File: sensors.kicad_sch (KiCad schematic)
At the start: 98 parts, among them M1 CD74HC4067SM, M2 CD74HC4067SM, M3 CD74HC4067SM, M4 CD74HC4067SM, M5 CD74HC4067SM, M6 CD74HC4067SM

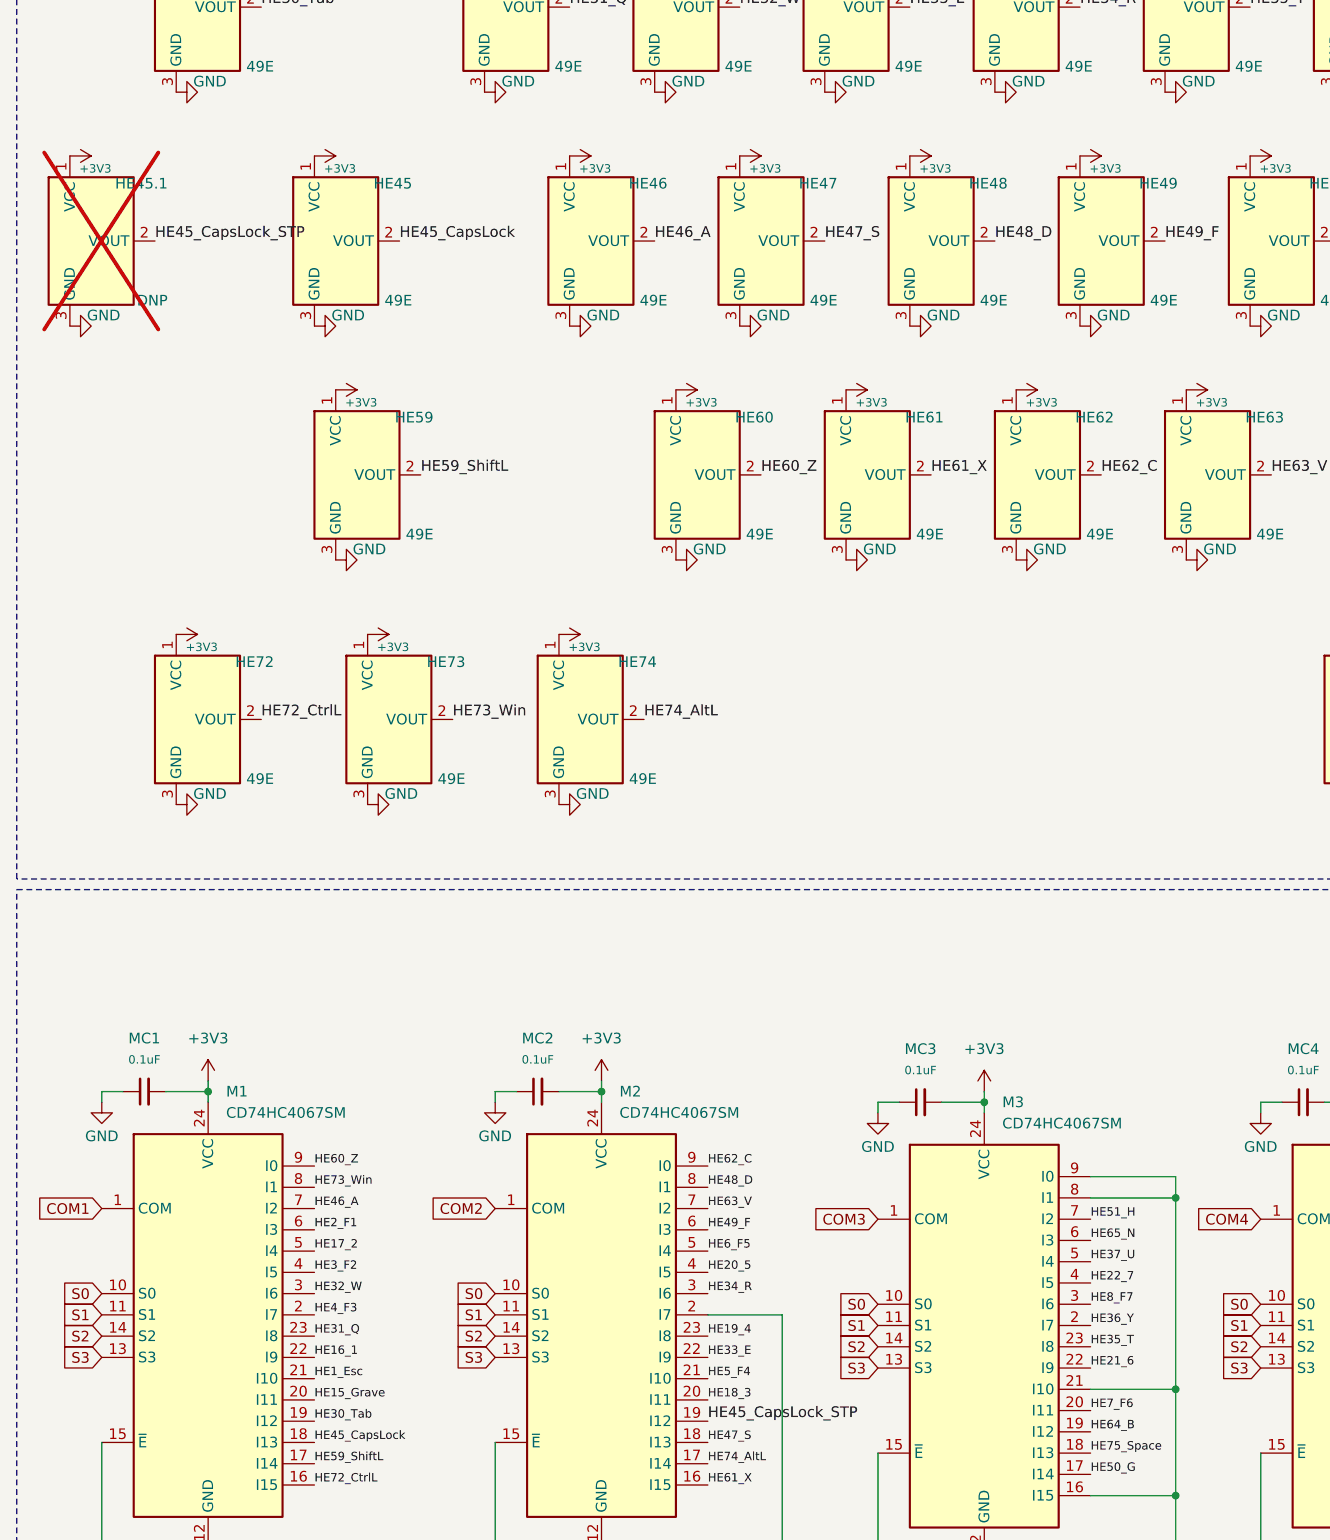
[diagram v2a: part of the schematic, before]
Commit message: VLT PCB rev: dual TFT connector, RKJXT1F42001 footprint, LED expansion header
- Add 12-pin TFT connector alongside existing 8-pin for CTP-integrated display option
- Superimpose RKJXT1F42001 5-way joystick footprint on EC11 encoder for testing
- Add LED expansion header for additional RGB zones
- Update production files
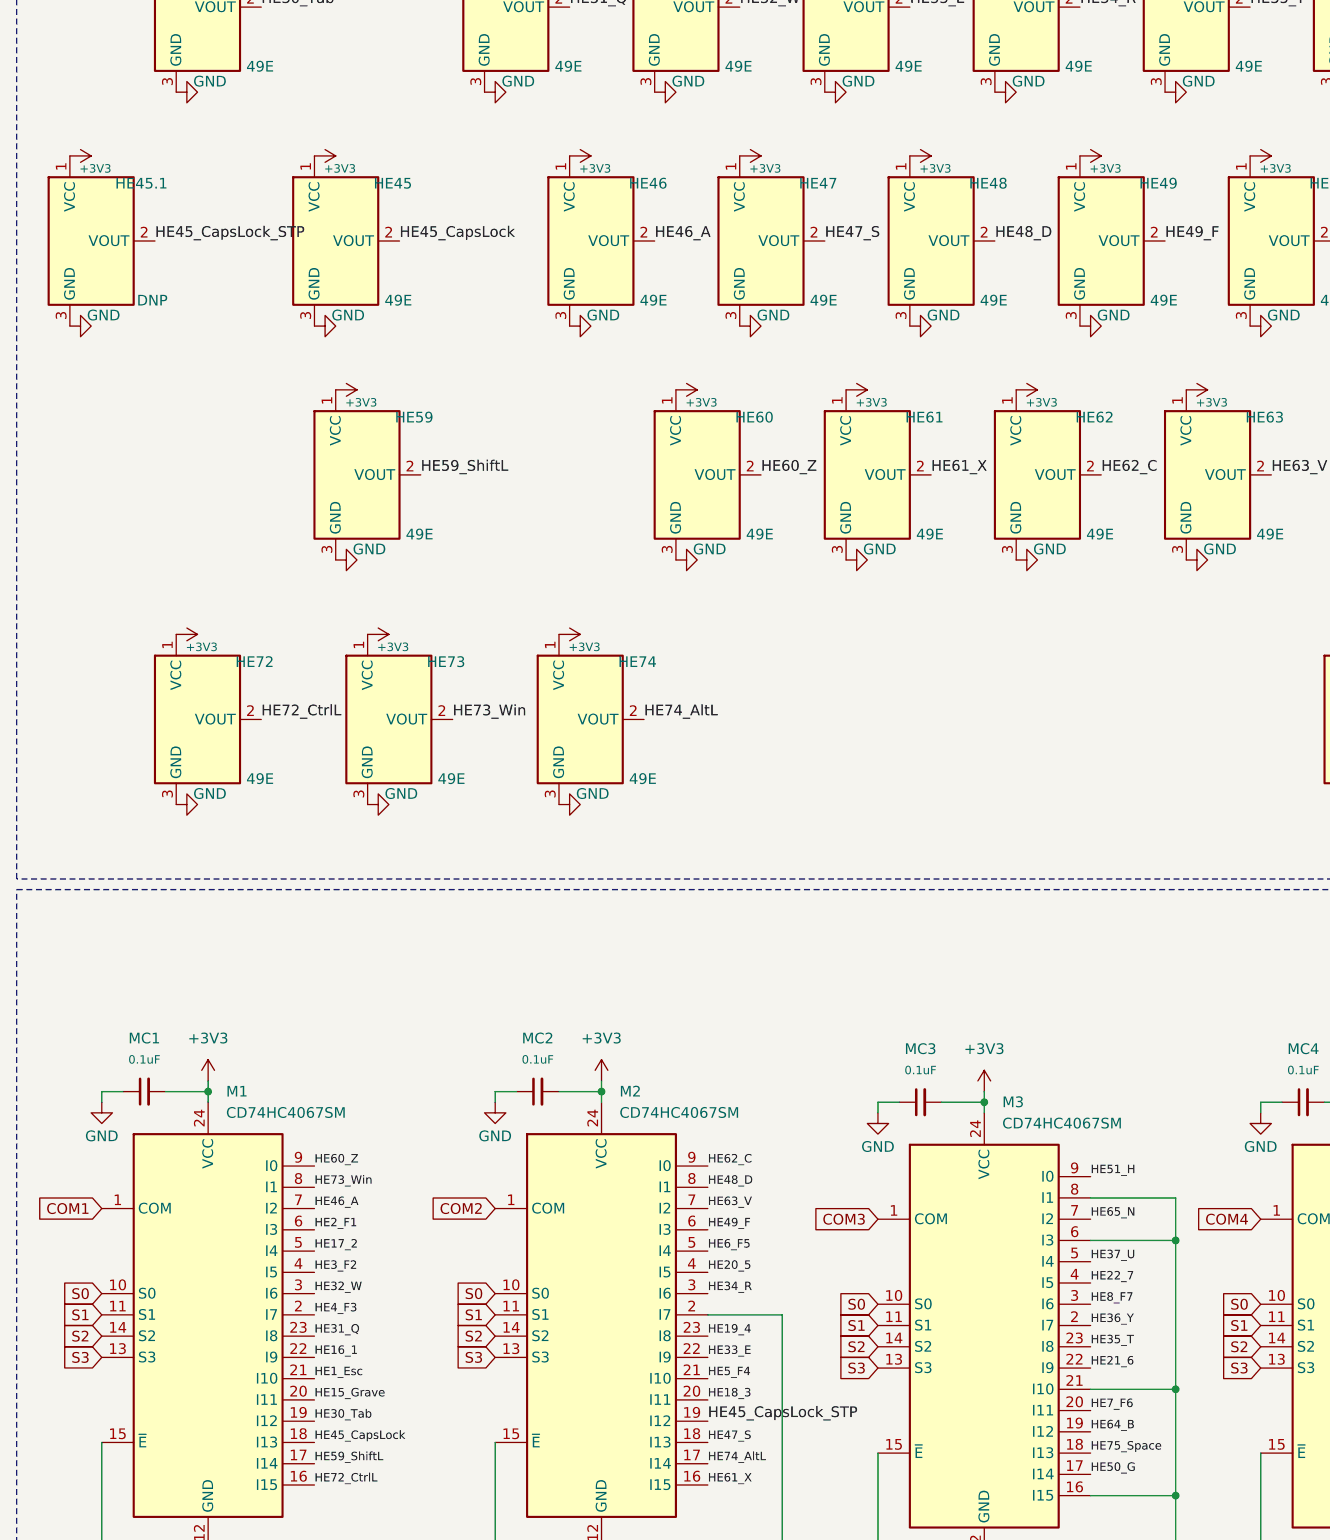
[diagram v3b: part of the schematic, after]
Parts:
- HE45.1: now fitted
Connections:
- net GND: now also M3.6 (I3); no longer M3.9 (I0)
- net HE51_H: now also M3.9 (I0); no longer M3.7 (I2)
- net HE65_N: now also M3.7 (I2); no longer M3.6 (I3)
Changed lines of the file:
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@@
 	)
 	(junction
-		(at 152.4 224.79)
-		(diameter 0)
-		(color 0 0 0 0)
-	)
-	(junction
 		(at 129.54 267.97)
 		(diameter 0)
@@
 	)
 	(junction
+		(at 152.4 229.87)
+		(diameter 0)
+		(color 0 0 0 0)
+	)
+	(junction
 		(at 196.85 227.33)
 		(diameter 0)
@@
 	(wire
 		(pts
-			(xy 152.4 222.25) (xy 152.4 224.79)
-		)
-		(stroke
-			(width 0)
-			(type default)
-		)
-	)
-	(wire
-		(pts
 			(xy 196.85 276.86) (xy 196.85 257.81)
 		)
@@
 	(wire
 		(pts
-			(xy 142.24 222.25) (xy 152.4 222.25)
-		)
-		(stroke
-			(width 0)
-			(type default)
-		)
-	)
-	(wire
-		(pts
 			(xy 96.52 238.76) (xy 105.41 238.76)
 		)
@@
 	(wire
 		(pts
+			(xy 142.24 229.87) (xy 152.4 229.87)
+		)
+		(stroke
+			(width 0)
+			(type default)
+		)
+	)
+	(wire
+		(pts
+			(xy 152.4 229.87) (xy 152.4 247.65)
+		)
+		(stroke
+			(width 0)
+			(type default)
+		)
+	)
+	(wire
+		(pts
 			(xy 162.56 267.97) (xy 175.26 267.97)
 		)
@@
 	(wire
 		(pts
-			(xy 152.4 224.79) (xy 152.4 247.65)
+			(xy 152.4 224.79) (xy 152.4 229.87)
 		)
 		(stroke
@@
 		)
 	)
+	(label "HE65_N"
+		(at 142.24 227.33 0)
+		(effects
+			(font
+				(size 1 1)
+			)
+			(justify left bottom)
+		)
+	)
 	(label "HE36_Y"
 		(at 181.61 82.55 0)
@@
 		)
 	)
-	(label "HE51_H"
-		(at 142.24 227.33 0)
-		(effects
-			(font
-				(size 1 1)
-			)
-			(justify left bottom)
-		)
-	)
 	(label "HE24_9"
 		(at 314.96 214.63 0)
@@
 		)
 	)
+	(label "HE51_H"
+		(at 142.24 222.25 0)
+		(effects
+			(font
+				(size 1 1)
+			)
+			(justify left bottom)
+		)
+	)
 	(label "HE32_W"
 		(at 49.53 236.22 0)
@@
 		)
 	)
-	(label "HE65_N"
-		(at 142.24 229.87 0)
-		(effects
-			(font
-				(size 1 1)
-			)
-			(justify left bottom)
-		)
-	)
 	(label "HE30_Tab"
 		(at 43.18 82.55 0)
@@
 		(in_bom yes)
 		(on_board yes)
-		(dnp yes)
+		(dnp no)
 		(property "Reference" "HE45.1"
 			(at 32.004 103.632 0)

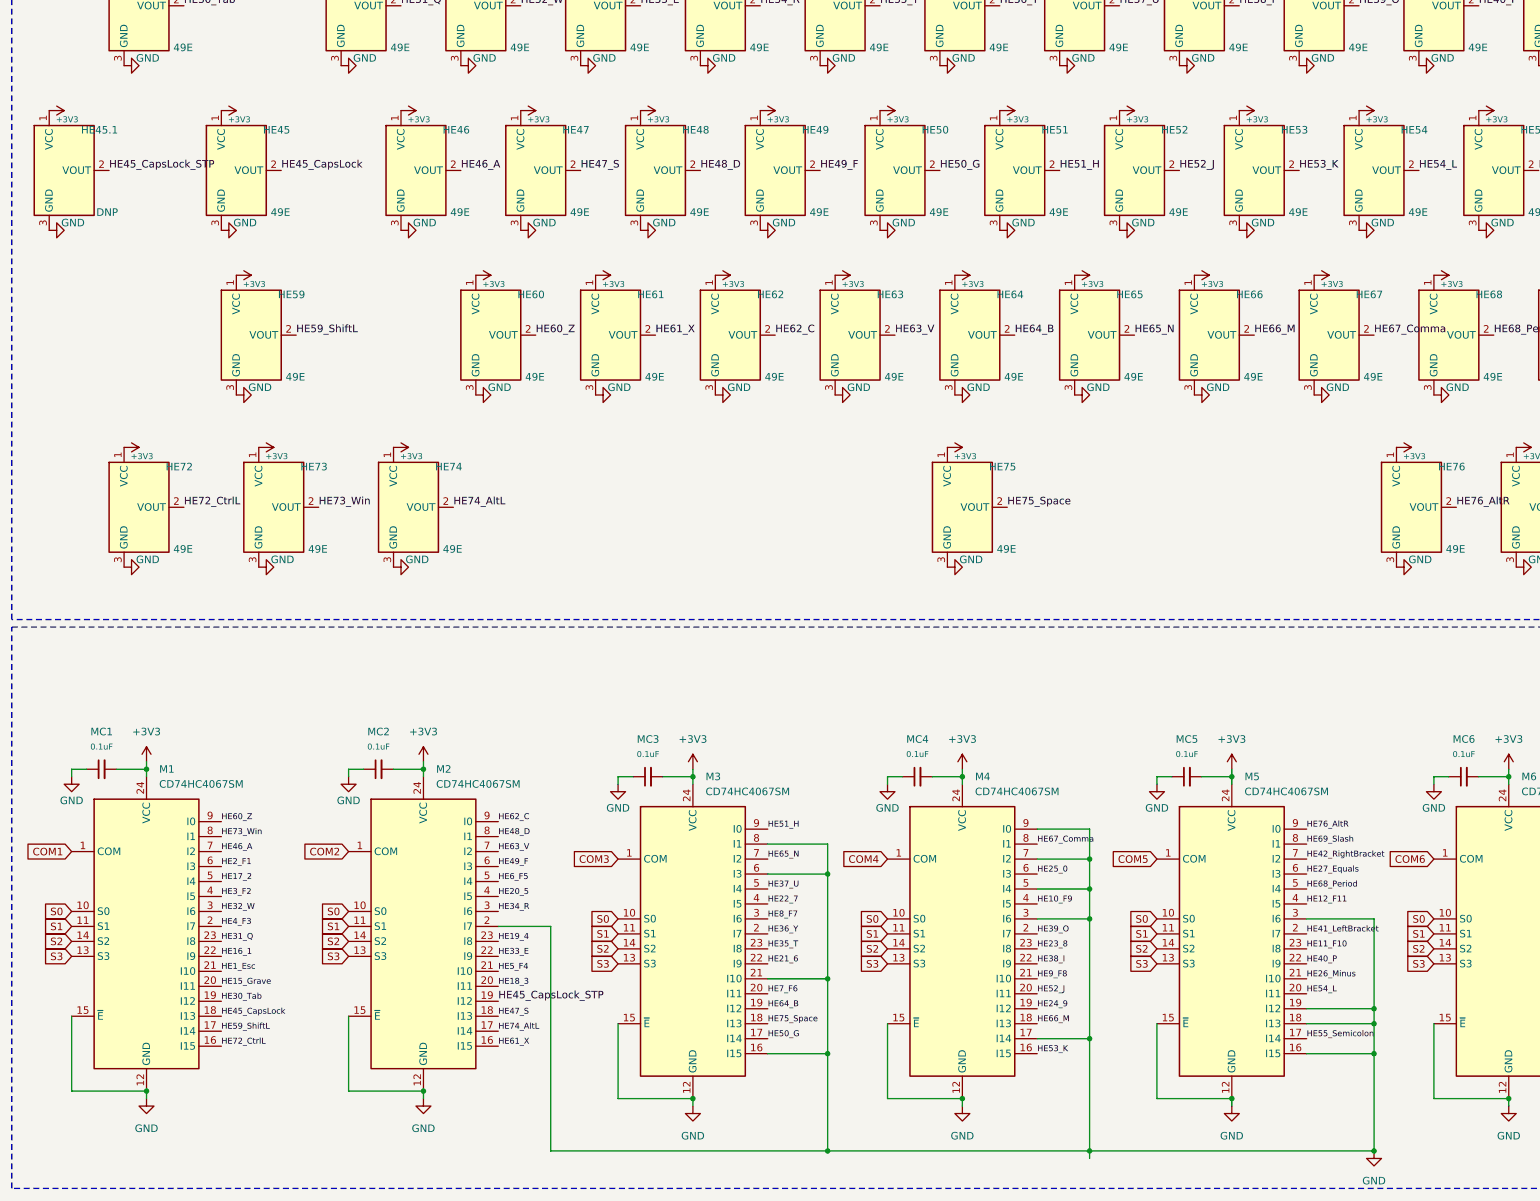
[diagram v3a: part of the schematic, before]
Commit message: PCB rev1 done — schematic/layout updates, drop stale production exports
- Schematic + PCB updates across VLT.kicad_pcb/sch, leds.kicad_sch, sensors.kicad_sch
- Remove production/ rev1 exports (zip/bom/positions/netlist) — regenerated on demand
- Drop fabrication-toolkit-options.json (not used)
- gitignore VLT+Dev/ experimental layouts
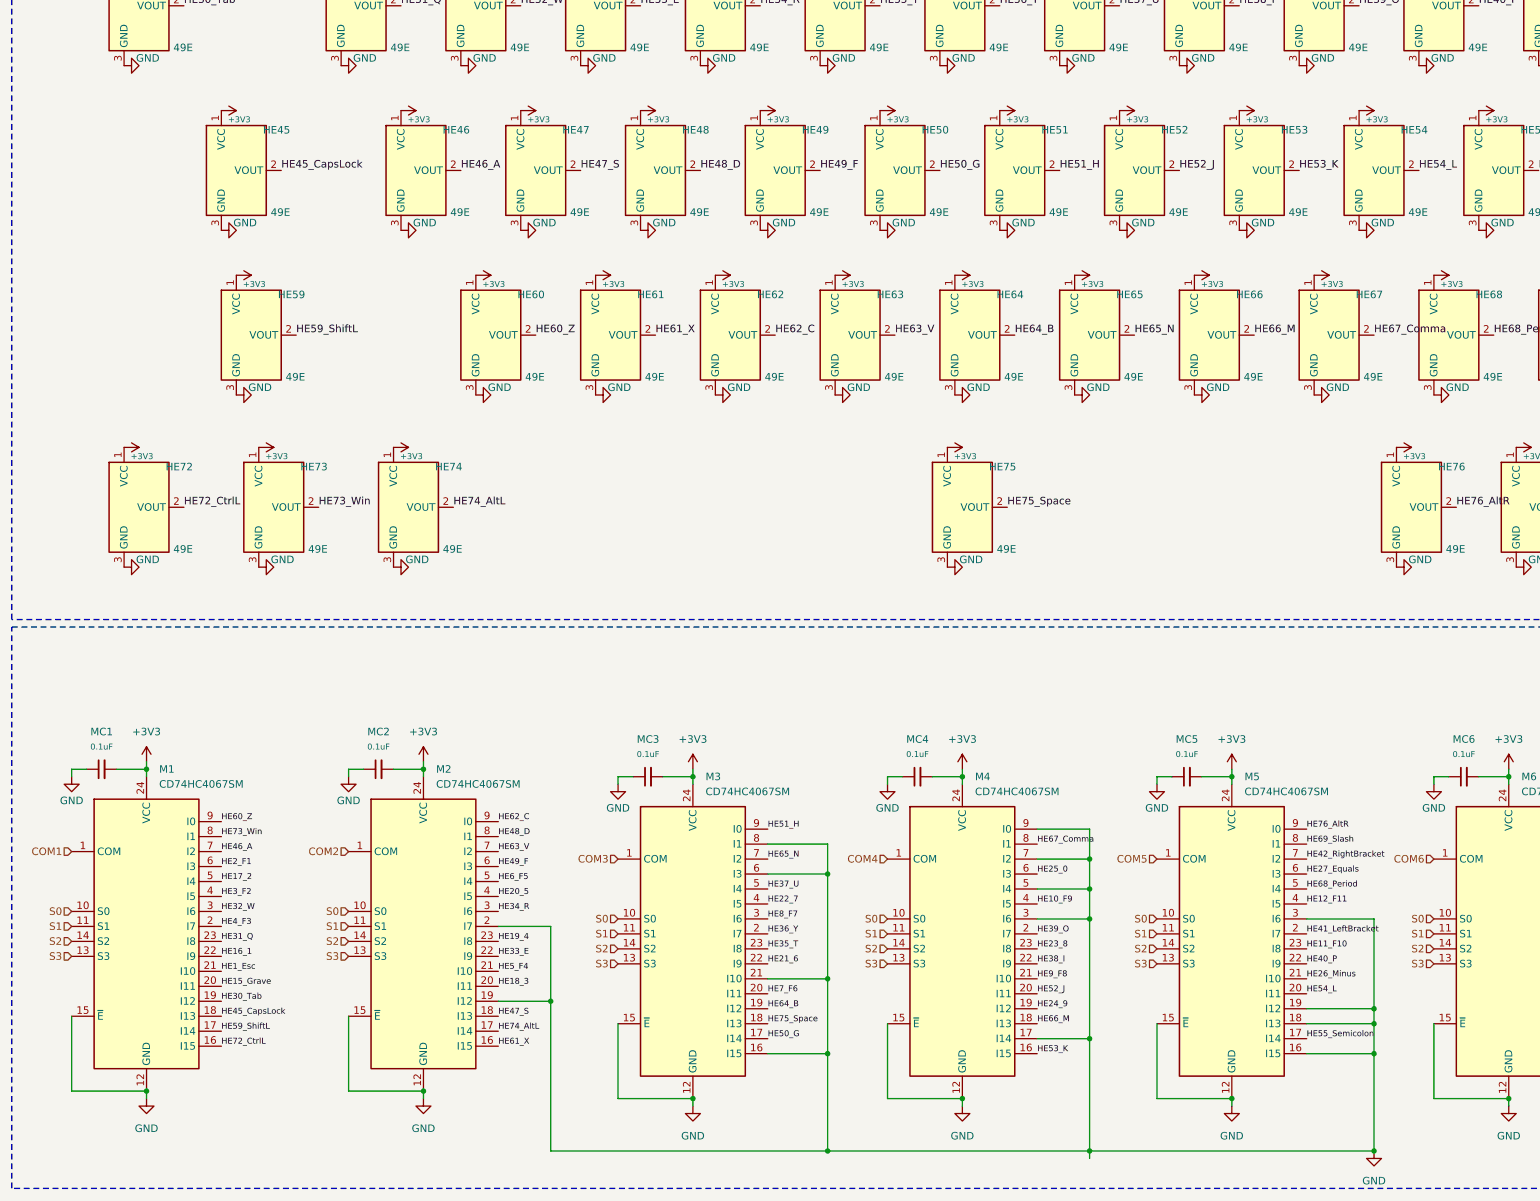
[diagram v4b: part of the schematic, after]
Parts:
- removed HE45.1: DNP, PCM_marbastlib-xp-he:SW_MX_HE_90deg_1.75u_STP_1.5_4layer, symbol PCM_marbastlib-he:SW_MX_HE
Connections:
- net HE45_CapsLock_STP is gone; now on net GND: M2.19 (I12)
